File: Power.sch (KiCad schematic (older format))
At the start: 7 parts, among them U3 L78L12_SOT89, U4 LP2985-3.3

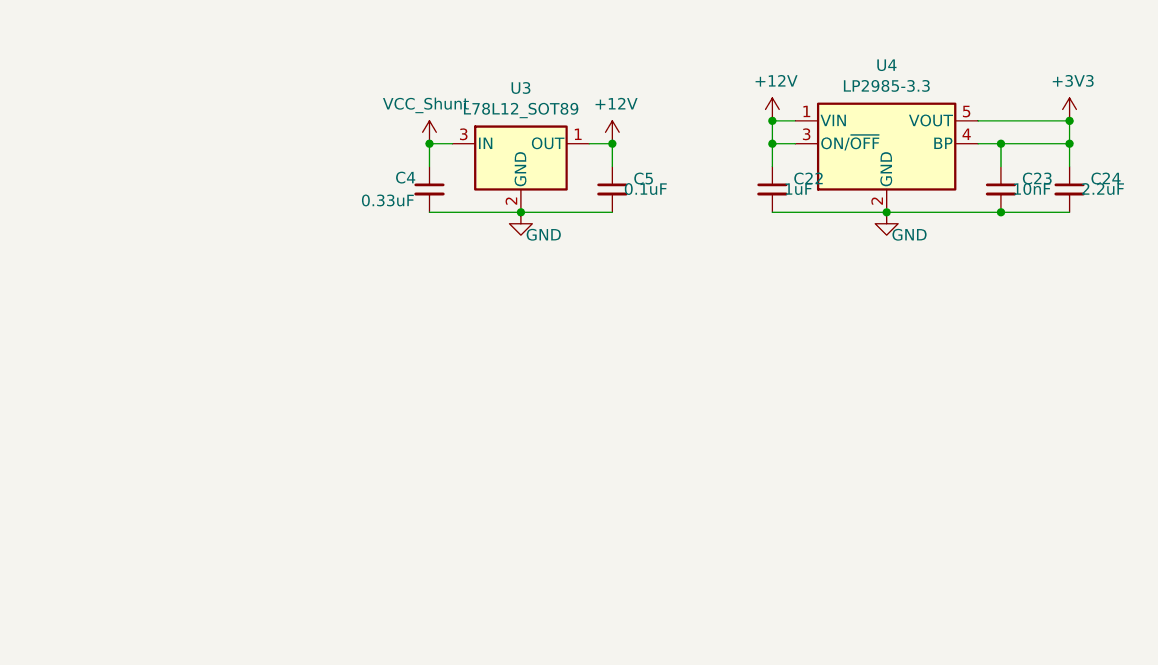
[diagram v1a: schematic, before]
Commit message: Addition of 5V Regulator
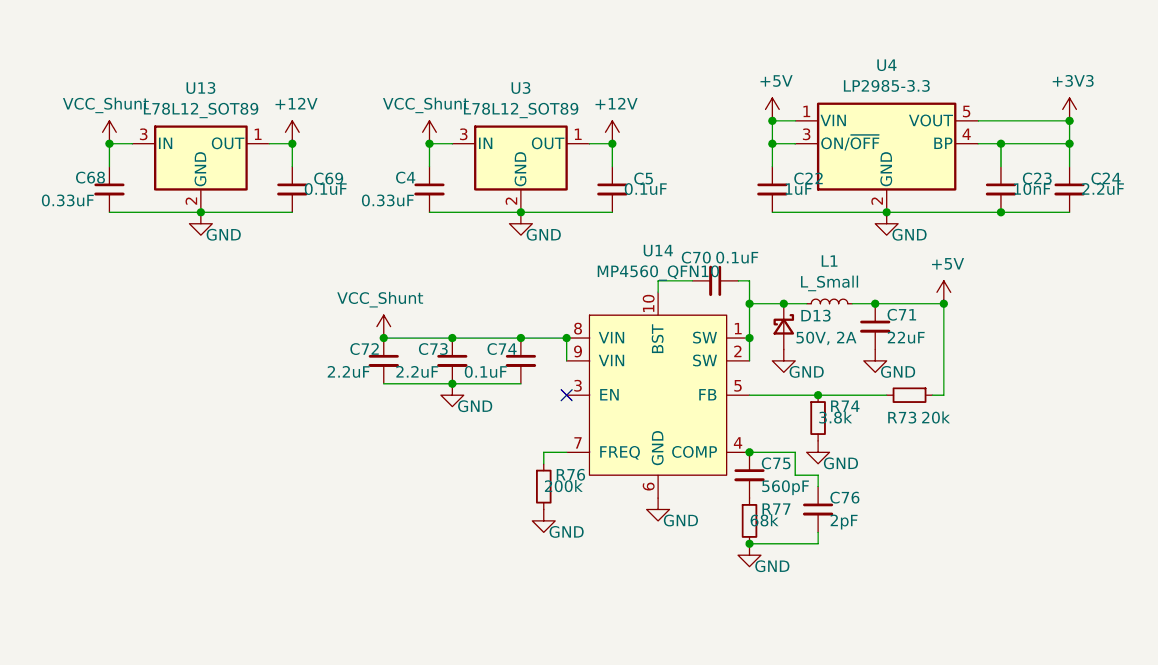
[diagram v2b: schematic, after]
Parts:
- added C68: 0.33uF, Capacitor_SMD:C_0603_1608Metric, symbol Device:C_Small
- added C69, C70: 0.1uF, Capacitor_SMD:C_0603_1608Metric, symbol Device:C_Small
- added C71: 22uF, Capacitor_SMD:C_0603_1608Metric, symbol Device:C_Small
- added C72, C73: 2.2uF, Capacitor_SMD:C_0603_1608Metric, symbol Device:C_Small
- added C74: 0.1uF, Capacitor_SMD:C_0402_1005Metric, symbol Device:C_Small
- added C75: 560pF, Capacitor_SMD:C_0402_1005Metric, symbol Device:C_Small
- added C76: 2pF, Capacitor_SMD:C_0402_1005Metric, symbol Device:C_Small
- added D13: 50V, 2A, Diode_SMD:D_SOD-123F, symbol Device:D_Schottky_Small
- added L1: L_Small, Inductor_SMD:L_Bourns-SRN5020, symbol Device:L_Small
- added R73: 20k, Resistor_SMD:R_0402_1005Metric, symbol Device:R_Small
- added R74: 3.8k, Resistor_SMD:R_0402_1005Metric, symbol Device:R_Small
- added R76: 200k, Resistor_SMD:R_0402_1005Metric, symbol Device:R_Small
- added R77: 68k, Resistor_SMD:R_0402_1005Metric, symbol Device:R_Small
- added U13: L78L12_SOT89, Package_TO_SOT_SMD:SOT-89-3, symbol Regulator_Linear:L78L12_SOT89
- added U14: MP4560_QFN10, Package_DFN_QFN:DFN-10-1EP_3x3mm_P0.5mm_EP1.7x2.5mm, symbol Regulator_Switching:MP4560_QFN10
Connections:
- net +12V: now also C69.1, U13.1 (OUT); no longer C22.1, U4.1 (VIN), U4.3 (ON/~OFF~)
- net GND: now also C68.2, C69.2, C71.2, C72.2, C73.2, C74.2, C76.2, D13.2 (A), R74.2, R76.2, R77.2, U13.2 (GND), U14.6 (GND)
- net VCC_Shunt: now also C68.1, C72.1, C73.1, C74.1, U13.3 (IN), U14.8 (VIN), U14.9 (VIN)
- new net: R76.1, U14.7 (FREQ)
- new net: C75.1, C76.1, U14.4 (COMP)
- new net: C75.2, R77.1
- new net: C70.1, D13.1 (K), L1.1, U14.1 (SW), U14.2 (SW)
- new net: C70.2, U14.10 (BST)
- new net: R73.2, R74.1, U14.5 (FB)
- new net +5V: C22.1, C71.1, L1.2, R73.1, U4.1 (VIN), U4.3 (ON/~OFF~)
- no-connect marks 0 -> 1

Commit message: Added 3V3 regulator and connected it to rest of board
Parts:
- C22: footprint Capacitor_SMD:C_0603_1608Metric -> Capacitor_SMD:C_0402_1005Metric
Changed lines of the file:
@@
 F 0 "C22" H 7642 3846 50  0000 L CNN
 F 1 "1uF" H 7600 3800 50  0000 L CNN
-F 2 "Capacitor_SMD:C_0603_1608Metric" H 7550 3800 50  0001 C CNN
+F 2 "Capacitor_SMD:C_0402_1005Metric" H 7550 3800 50  0001 C CNN
 F 3 "~" H 7550 3800 50  0001 C CNN
 	1    7550 3800

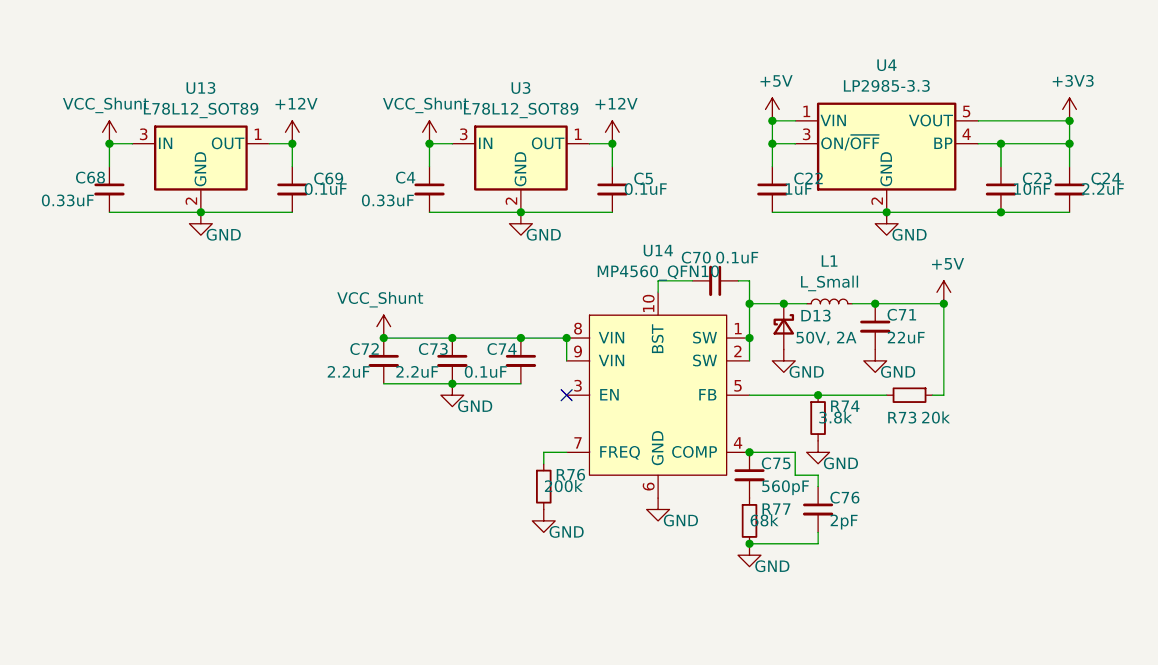
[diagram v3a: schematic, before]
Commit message: Finished all traces and vias
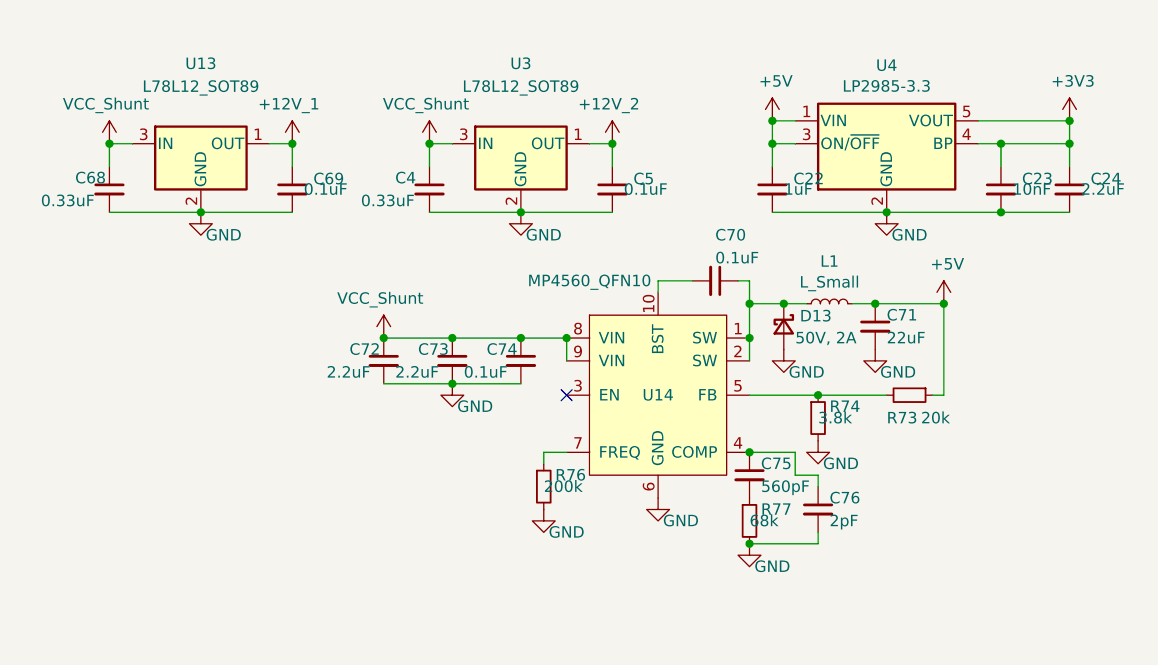
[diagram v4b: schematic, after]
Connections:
- net +12V renamed +12V_1
- net +12V_1: no longer C5.1, U3.1 (OUT)
- new net +12V_2: C5.1, U3.1 (OUT)
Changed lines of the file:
@@
 $EndComp
-$Comp
-L power:+12V #PWR0105
-U 1 1 603EEDC9
-P 6850 3600
-F 0 "#PWR0105" H 6850 3450 50  0001 C CNN
-F 1 "+12V" H 6865 3773 50  0000 C CNN
-F 2 "" H 6850 3600 50  0001 C CNN
-F 3 "" H 6850 3600 50  0001 C CNN
-	1    6850 3600
-	1    0    0    -1
-$EndComp
-Connection ~ 6850 3600
 $Comp
 L power:VCC_Shunt #PWR0128
@@
 U 1 1 604B9DDC
 P 6450 3600
-F 0 "U3" H 6450 3842 50  0000 C CNN
-F 1 "L78L12_SOT89" H 6450 3751 50  0000 C CNN
+F 0 "U3" H 6450 3950 50  0000 C CNN
+F 1 "L78L12_SOT89" H 6450 3850 50  0000 C CNN
 F 2 "Package_TO_SOT_SMD:SOT-89-3" H 6450 3800 50  0001 C CIN
 F 3 "http://www.st.com/content/ccc/resource/technical/document/datasheet/15/55/e5/aa/23/5b/43/fd/CD00000446.pdf/files/CD00000446.pdf/jcr:content/translations/en.CD00000446.pdf" H 6450 3550 50  0001 C CNN
@@
 $EndComp
 $Comp
-L power:+12V #PWR0102
-U 1 1 60527FFD
-P 5450 3600
-F 0 "#PWR0102" H 5450 3450 50  0001 C CNN
-F 1 "+12V" H 5465 3773 50  0000 C CNN
-F 2 "" H 5450 3600 50  0001 C CNN
-F 3 "" H 5450 3600 50  0001 C CNN
-	1    5450 3600
-	1    0    0    -1
-$EndComp
-Connection ~ 5450 3600
-$Comp
 L power:VCC_Shunt #PWR0134
 U 1 1 60528004
@@
 U 1 1 6052800B
 P 5050 3600
-F 0 "U13" H 5050 3842 50  0000 C CNN
-F 1 "L78L12_SOT89" H 5050 3751 50  0000 C CNN
+F 0 "U13" H 5050 3950 50  0000 C CNN
+F 1 "L78L12_SOT89" H 5050 3850 50  0000 C CNN
 F 2 "Package_TO_SOT_SMD:SOT-89-3" H 5050 3800 50  0001 C CIN
 F 3 "http://www.st.com/content/ccc/resource/technical/document/datasheet/15/55/e5/aa/23/5b/43/fd/CD00000446.pdf/files/CD00000446.pdf/jcr:content/translations/en.CD00000446.pdf" H 5050 3550 50  0001 C CNN
@@
 AR Path="/605E7573" Ref="C?"  Part="1"
 AR Path="/60308500/605E7573" Ref="C70"  Part="1"
-F 0 "C70" V 7200 4050 50  0000 L CNN
+F 0 "C70" V 7100 4200 50  0000 L CNN
 F 1 "0.1uF" V 7200 4200 50  0000 L CNN
 F 2 "Capacitor_SMD:C_0603_1608Metric" H 7300 4200 50  0001 C CNN
@@
 U 1 1 60632F9F
 P 7050 4700
-F 0 "U14" H 7050 5331 50  0000 C CNN
-F 1 "MP4560_QFN10" H 7050 5240 50  0000 C CNN
+F 0 "U14" H 7050 4700 50  0000 C CNN
+F 1 "MP4560_QFN10" H 6750 5200 50  0000 C CNN
 F 2 "Package_DFN_QFN:DFN-10-1EP_3x3mm_P0.5mm_EP1.7x2.5mm" H 7050 5000 50  0001 C CNN
 F 3 "" H 7050 5000 50  0001 C CNN
@@
 	7450 4550 7450 4450
 Connection ~ 7450 4450
+$Comp
+L power:+12V_1 #PWR0102
+U 1 1 606EA907
+P 5450 3600
+F 0 "#PWR0102" H 5450 3500 50  0001 C CNN
+F 1 "+12V_1" H 5435 3773 50  0000 C CNN
+F 2 "" H 5450 3600 50  0001 C CNN
+F 3 "" H 5450 3600 50  0001 C CNN
+	1    5450 3600
+	1    0    0    -1
+$EndComp
+Connection ~ 5450 3600
+$Comp
+L power:+12V_2 #PWR0105
+U 1 1 606EB97F
+P 6850 3600
+F 0 "#PWR0105" H 6850 3550 50  0001 C CNN
+F 1 "+12V_2" H 6835 3773 50  0000 C CNN
+F 2 "" H 6850 3600 50  0001 C CNN
+F 3 "" H 6850 3600 50  0001 C CNN
+	1    6850 3600
+	1    0    0    -1
+$EndComp
+Connection ~ 6850 3600
 $EndSCHEMATC

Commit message: Added more PNGs
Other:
- note added: "12V LDO Regulators"
- note added: "3V3 LDO Regulator"
- note added: "5V SMPS Regulator"
- moved on the sheet: C22, C23, C24, C70, C71, C72, C73, C74, C75, C76, D13, L1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
